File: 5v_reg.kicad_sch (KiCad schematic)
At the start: 13 parts, among them U3 IR3899A

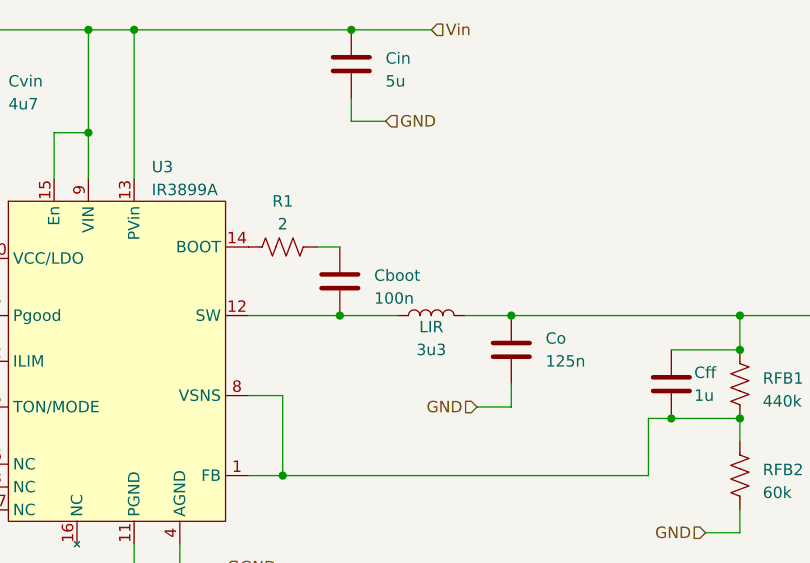
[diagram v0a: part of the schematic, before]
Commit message: Added extra output capacitance to 12V regulator, added component designators
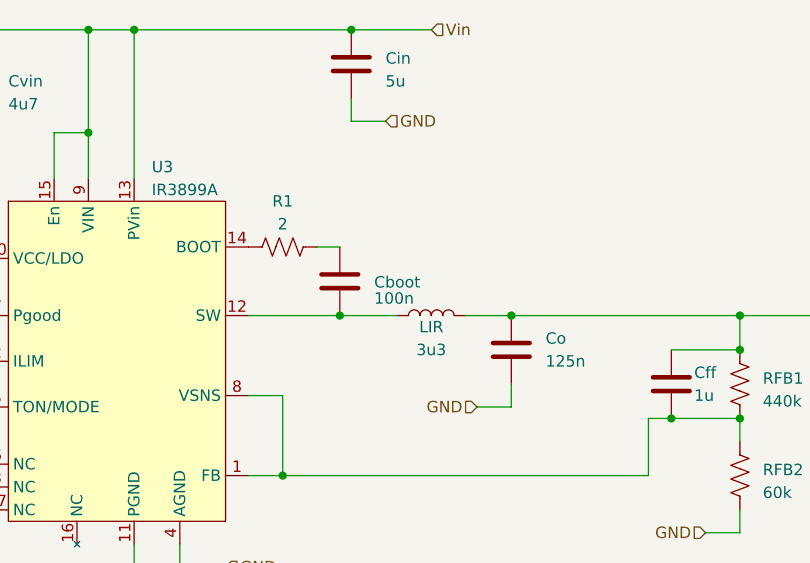
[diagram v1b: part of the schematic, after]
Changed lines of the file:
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@@
   )
   (symbol (lib_id "Device:C") (at 158.75 87.63 0) (unit 1)
-    (in_bom yes) (on_board yes) (dnp no) (fields_autoplaced)
+    (in_bom yes) (on_board yes) (dnp no)
     (property "Reference" "Cboot" (at 162.56 86.995 0)
-      (effects (font (size 1.27 1.27)) (justify left))
+      (effects (font (size 1.27 1.27)) (justify left top))
     )
     (property "Value" "100n" (at 162.56 89.535 0)
@@
         )
         (path "/530b9f5d-4c5f-47a4-a889-3cce870d311f/66b48989-026d-4927-b86c-76e19138a6ff"
-          (reference "Cboot2") (unit 1)
+          (reference "C20") (unit 1)
         )
       )
@@
         )
         (path "/530b9f5d-4c5f-47a4-a889-3cce870d311f/66b48989-026d-4927-b86c-76e19138a6ff"
-          (reference "Cff1") (unit 1)
+          (reference "C23") (unit 1)
         )
       )
@@
         )
         (path "/530b9f5d-4c5f-47a4-a889-3cce870d311f/66b48989-026d-4927-b86c-76e19138a6ff"
-          (reference "Cin2") (unit 1)
+          (reference "C21") (unit 1)
         )
       )
@@
         )
         (path "/530b9f5d-4c5f-47a4-a889-3cce870d311f/66b48989-026d-4927-b86c-76e19138a6ff"
-          (reference "Cvin1") (unit 1)
+          (reference "C19") (unit 1)
         )
       )
@@
         )
         (path "/530b9f5d-4c5f-47a4-a889-3cce870d311f/66b48989-026d-4927-b86c-76e19138a6ff"
-          (reference "RFB1") (unit 1)
+          (reference "R23") (unit 1)
         )
       )
@@
         )
         (path "/530b9f5d-4c5f-47a4-a889-3cce870d311f/66b48989-026d-4927-b86c-76e19138a6ff"
-          (reference "RFB2") (unit 1)
+          (reference "R24") (unit 1)
         )
       )
@@
         )
         (path "/530b9f5d-4c5f-47a4-a889-3cce870d311f/66b48989-026d-4927-b86c-76e19138a6ff"
-          (reference "Co1") (unit 1)
+          (reference "C22") (unit 1)
         )
       )
@@
         )
         (path "/530b9f5d-4c5f-47a4-a889-3cce870d311f/66b48989-026d-4927-b86c-76e19138a6ff"
-          (reference "Cvcc1") (unit 1)
+          (reference "C18") (unit 1)
         )
       )
@@
         )
         (path "/530b9f5d-4c5f-47a4-a889-3cce870d311f/66b48989-026d-4927-b86c-76e19138a6ff"
-          (reference "LIR1") (unit 1)
+          (reference "L4") (unit 1)
         )
       )
@@
         )
         (path "/530b9f5d-4c5f-47a4-a889-3cce870d311f/66b48989-026d-4927-b86c-76e19138a6ff"
-          (reference "COHF1") (unit 1)
+          (reference "C24") (unit 1)
         )
       )
@@
         )
         (path "/530b9f5d-4c5f-47a4-a889-3cce870d311f/66b48989-026d-4927-b86c-76e19138a6ff"
-          (reference "Rpg1") (unit 1)
-        )
-      )
+          (reference "R22") (unit 1)
+        )
+      )

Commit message: Added more component footprints
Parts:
- U3: footprint (none) -> crush-power-footprints:IR3899AMTRPBFAUMA1
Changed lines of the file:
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@@
       (effects (font (size 1.27 1.27)) (justify left))
     )
-    (property "Footprint" "" (at 130.81 78.74 0)
+    (property "Footprint" "crush-power-footprints:IR3899AMTRPBFAUMA1" (at 130.81 78.74 0)
       (effects (font (size 1.27 1.27)) hide)
     )
-    (property "Datasheet" "" (at 130.81 78.74 0)
+    (property "Datasheet" "https://www.infineon.com/dgdl/Infineon-IR3899AMTRPBF-DataSheet-v02_30-EN.pdf?fileId=5546d46276fb756a0177072216135f1f" (at 130.81 78.74 0)
       (effects (font (size 1.27 1.27)) hide)
     )

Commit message: Fixed a lot of components
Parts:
- removed COHF: 100n, symbol Device:C
- added C24, C29, C30: 47u, Capacitor_SMD:C_0805_2012Metric_Pad1.18x1.45mm_HandSolder, symbol Device:C
- added C25, C26, C27, C28: 22u, Capacitor_SMD:C_0805_2012Metric_Pad1.18x1.45mm_HandSolder, symbol Device:C
- Cff: value 1u -> 4u7; footprint (none) -> Capacitor_SMD:C_0603_1608Metric_Pad1.08x0.95mm_HandSolder
- LIR: value 3u3 -> 2u8; footprint (none) -> crush-power-footprints:IND_1365-WE-HCI_WRE-L
- R1: value 2 -> 2R; footprint (none) -> Resistor_SMD:R_0201_0603Metric
- RFB1, RFB2, Rpg: footprint (none) -> Resistor_SMD:R_0201_0603Metric
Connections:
- net 5V_OUT: now also C24.1, C29.1, C30.1
- net GND: now also C24.2, C25.2, C26.2, C27.2, C28.2, C29.2, C30.2
- net Vin: now also C25.1, C26.1, C27.1, C28.1
- no-connect marks 1 -> 5
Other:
- moved on the sheet: Cff, RFB1, RFB2

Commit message: Added extra footprints for diodes and capacitors
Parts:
- Cboot, Cin, Co, Cvcc, Cvin: footprint (none) -> Capacitor_SMD:C_0805_2012Metric_Pad1.18x1.45mm_HandSolder
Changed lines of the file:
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@@
       (effects (font (size 1.27 1.27)) (justify left))
     )
-    (property "Footprint" "" (at 159.7152 91.44 0)
+    (property "Footprint" "Capacitor_SMD:C_0805_2012Metric_Pad1.18x1.45mm_HandSolder" (at 159.7152 91.44 0)
       (effects (font (size 1.27 1.27)) hide)
     )
@@
       (effects (font (size 1.27 1.27)) (justify left))
     )
-    (property "Footprint" "" (at 160.9852 67.31 0)
+    (property "Footprint" "Capacitor_SMD:C_0805_2012Metric_Pad1.18x1.45mm_HandSolder" (at 160.9852 67.31 0)
       (effects (font (size 1.27 1.27)) hide)
     )
@@
       (effects (font (size 1.27 1.27)) (justify left))
     )
-    (property "Footprint" "" (at 119.0752 69.85 0)
+    (property "Footprint" "Capacitor_SMD:C_0805_2012Metric_Pad1.18x1.45mm_HandSolder" (at 119.0752 69.85 0)
       (effects (font (size 1.27 1.27)) hide)
     )
@@
       (effects (font (size 1.27 1.27)) (justify left))
     )
-    (property "Footprint" "" (at 178.7652 99.06 0)
+    (property "Footprint" "Capacitor_SMD:C_0805_2012Metric_Pad1.18x1.45mm_HandSolder" (at 178.7652 99.06 0)
       (effects (font (size 1.27 1.27)) hide)
     )
@@
       (effects (font (size 1.27 1.27)) (justify left))
     )
-    (property "Footprint" "" (at 110.1852 85.09 0)
-      (effects (font (size 1.27 1.27)) hide)
-    )
+    (property "Footprint" "Capacitor_SMD:C_0805_2012Metric_Pad1.18x1.45mm_HandSolder" (at 110.1852 85.09 0)
+      (effects (font (size 1.27 1.27)) hide)
+    )
